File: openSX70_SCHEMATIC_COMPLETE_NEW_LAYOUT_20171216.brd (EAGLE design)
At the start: 95.9 x 27.9 mm, 39 parts, among them Q1 5.8A/30V/35mΩ, Q2 5.8A/30V/35mΩ, U1 ATMEGA328P_TQFP, U3 BH1750FVI-TR, Y1 CSTCE16M0V53-R0

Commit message: new board work in progress.
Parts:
- moved Q1 117.0 mm to (72.4, 8.89)
- moved U1 110.7 mm to (81.3, 14.0), turned to 90 degrees
- moved R1 108.0 mm to (76.8, 4.83), turned to 180 degrees
- moved D1 99.9 mm to (77.5, 26.7), turned to 90 degrees
- moved R2 91.2 mm to (68.6, 2.54)
- moved CONN1 79.1 mm to (40.6, 2.54)
- moved R10 72.6 mm to (43.2, 26.7)
- moved C6 70.3 mm to (47.0, 26.7)
- moved R8 69.3 mm to (19.1, 8.89), flipped to the bottom, turned to 90 degrees
- moved LD11173.3V 66.3 mm to (36.8, 25.4), turned to 180 degrees
- moved R3 63.5 mm to (24.1, 3.81), turned to 90 degrees
- moved U3 63.4 mm to (18.9, 20.3), flipped to the bottom, turned to 270 degrees
- moved Y1 61.1 mm to (8.89, 7.62), turned to 270 degrees
- moved R4 54.0 mm to (24.1, 7.62), turned to 90 degrees
- moved LED1 46.0 mm to (19.1, 3.81), flipped to the bottom
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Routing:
- net 6V: track 0.00 -> 26.2 mm, vias 0 -> 2
- net S5: track 0.00 -> 12.0 mm
- net S3: track 0.00 -> 11.7 mm
- net S1: track 0.00 -> 7.27 mm

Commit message: small steps on the board.
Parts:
- moved C6 28.2 mm to (63.5, 3.81)
- moved LD11173.3V 27.9 mm to (11.4, 14.0)
- moved R1 9.19 mm to (67.7, 5.71), turned to 0 degrees
- moved Q1 4.58 mm to (74.9, 5.08), turned to 270 degrees
- moved R2 1.63 mm to (67.6, 3.81)
- moved CONN1 1.27 mm to (40.6, 3.81)
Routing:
- net GND: track 0.00 -> 13.7 mm
- net SOL1-: track 0.00 -> 6.64 mm, vias 0 -> 2

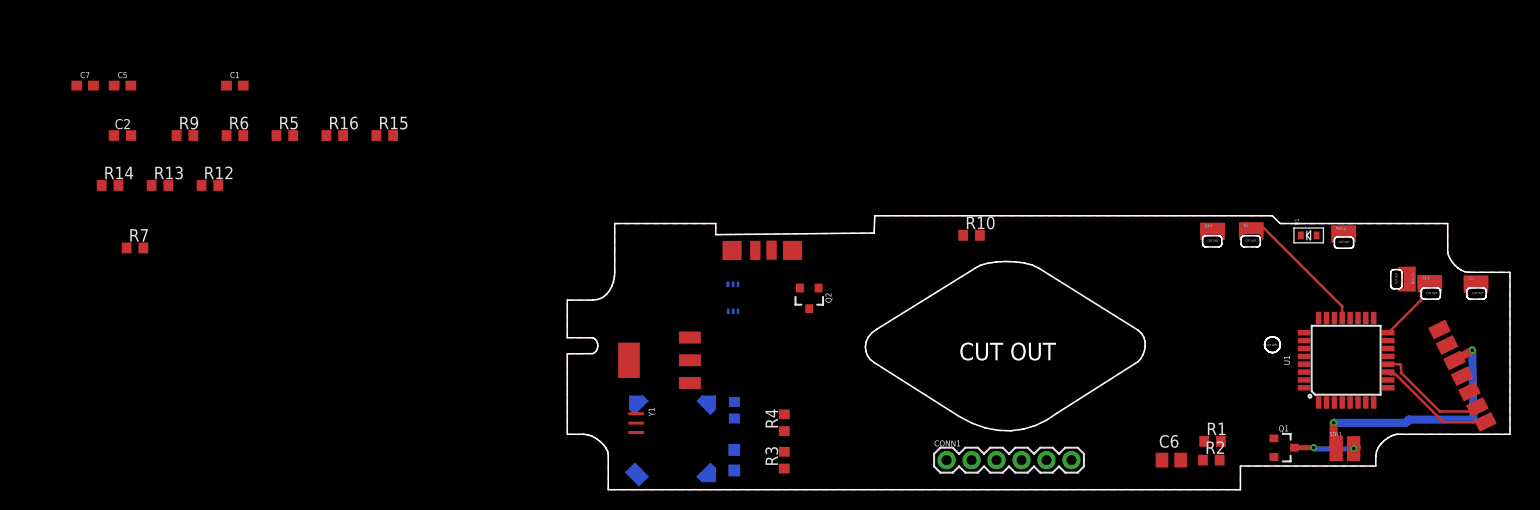
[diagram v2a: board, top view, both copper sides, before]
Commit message: Changed MOTOR pin from 19 to 25. The board is a mess and I have to start over.
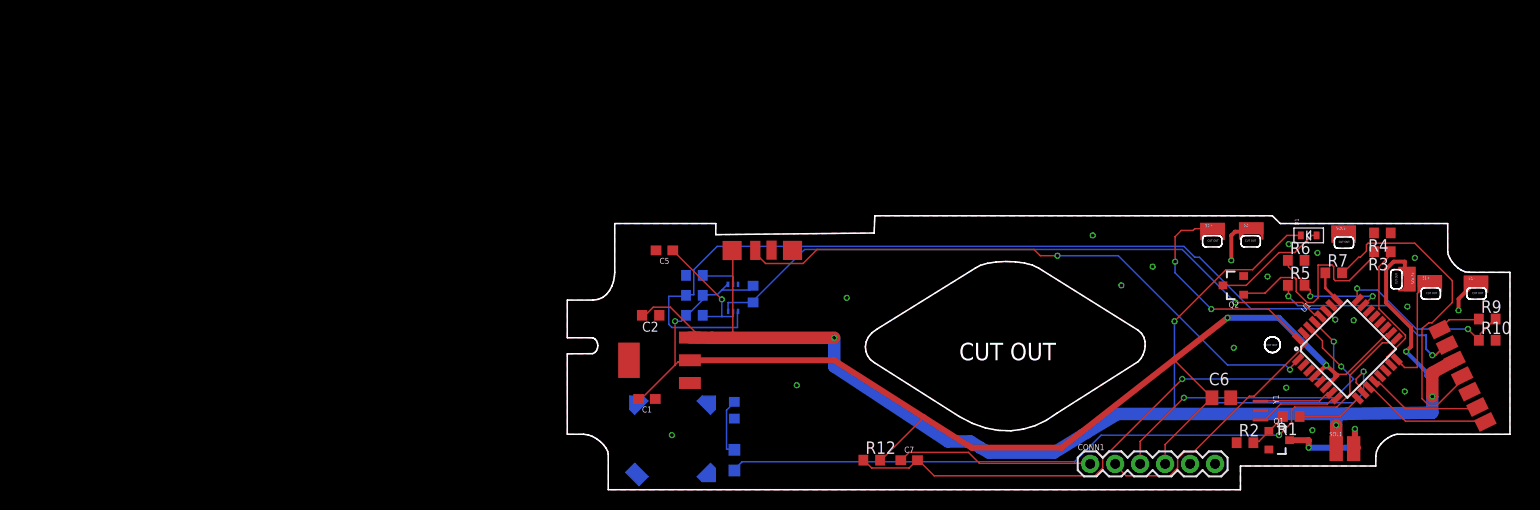
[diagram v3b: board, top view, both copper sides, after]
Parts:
- moved R9 133.8 mm to (95.6, 18.2)
- moved R7 121.9 mm to (80.0, 22.9)
- moved R6 108.7 mm to (76.2, 24.1)
- moved R5 104.0 mm to (76.2, 21.6)
- moved C7 92.1 mm to (36.8, 3.81)
- moved R12 72.9 mm to (33.0, 3.81)
- moved R3 64.4 mm to (85.0, 25.0), turned to 180 degrees
- moved R4 63.8 mm to (85.0, 26.9), turned to 180 degrees
- moved Y1 63.5 mm to (72.4, 8.89)
- moved R14 60.1 mm to (15.0, 22.6), flipped to the bottom
- moved C5 57.6 mm to (11.9, 25.1), turned to 180 degrees
- moved C2 56.7 mm to (10.5, 18.5), turned to 180 degrees
- moved R13 55.9 mm to (15.0, 18.5), flipped to the bottom
- moved R10 53.5 mm to (95.6, 16.0)
- moved C1 52.7 mm to (10.2, 10.0), turned to 180 degrees
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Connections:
- removed net MOTOR+: R7.1, U1.22
- new net MOTOR: R7.1, U1.25
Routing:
- net 6V: track 26.2 -> 155.9 mm, vias 2 -> 5
- net 3.3V: track 0.00 -> 128.7 mm, vias 0 -> 3
- net SDA: track 0.00 -> 87.5 mm, vias 0 -> 1
- net LED: track 0.00 -> 75.0 mm, vias 0 -> 1
- net SCL: track 0.00 -> 66.3 mm, vias 0 -> 1
- net FF: track 0.00 -> 62.1 mm, vias 0 -> 2
- net N$9: track 0.00 -> 60.4 mm, vias 0 -> 2
- net MOTOR-HEADER: track 0.00 -> 33.8 mm
- net RXD: track 0.00 -> 33.7 mm, vias 0 -> 2
- net TXD: track 0.00 -> 27.4 mm
- net S2: track 0.00 -> 23.1 mm, vias 0 -> 2
- net N$3: track 0.00 -> 22.2 mm
- net S9@6V: track 0.00 -> 21.1 mm, vias 0 -> 2
- net BUZZER: track 0.00 -> 20.5 mm, vias 0 -> 1
- net DTR: track 0.00 -> 20.1 mm
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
